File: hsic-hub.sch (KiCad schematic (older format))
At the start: 17 parts

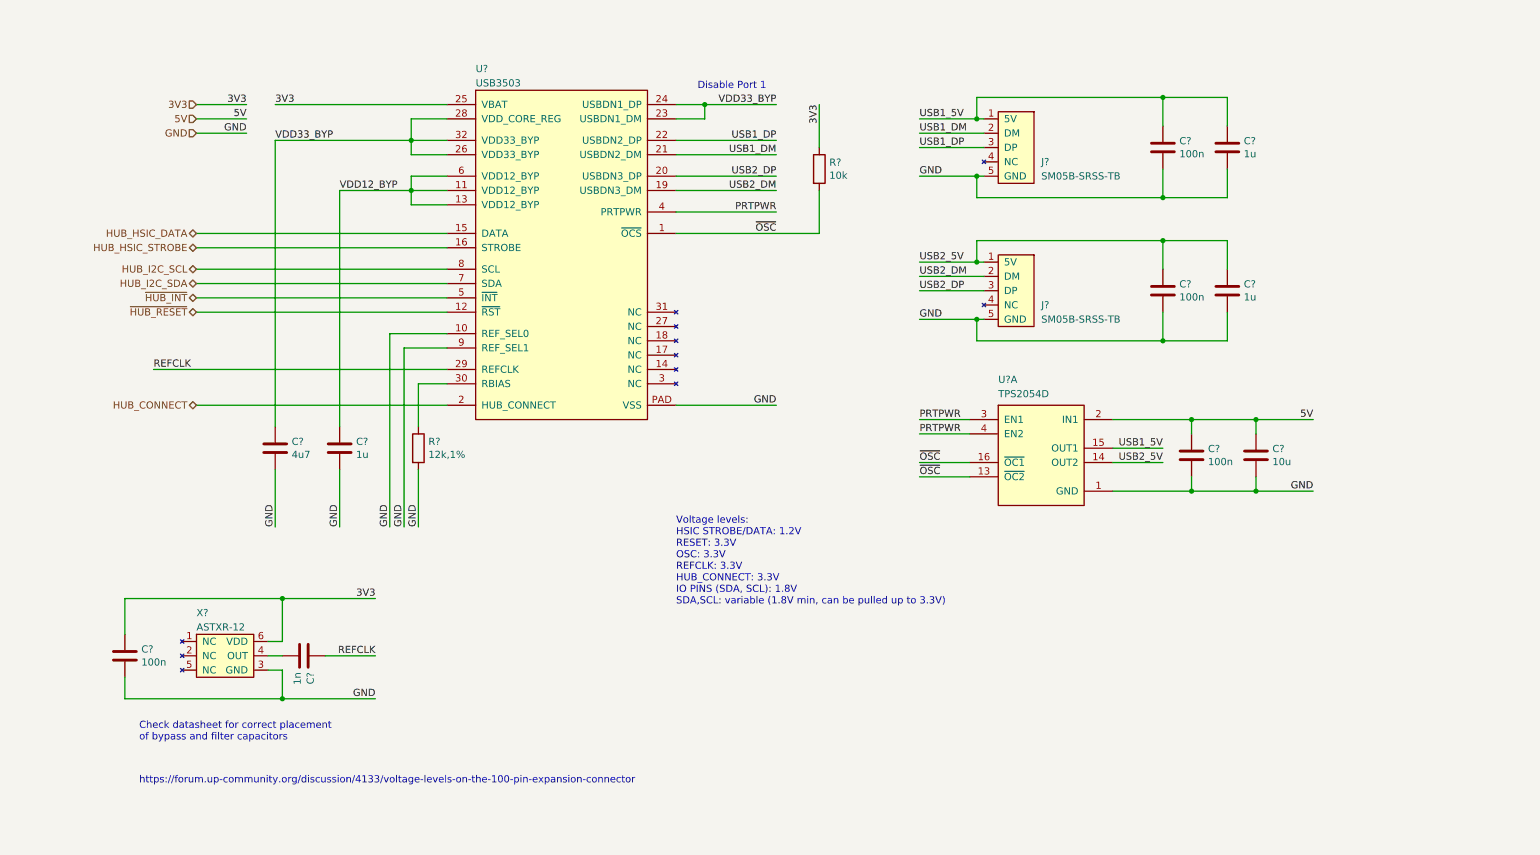
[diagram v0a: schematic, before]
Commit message: Multiple updates. 1. Add MOSFETs to libraries 2. Update HSIC schematic to include level shifting
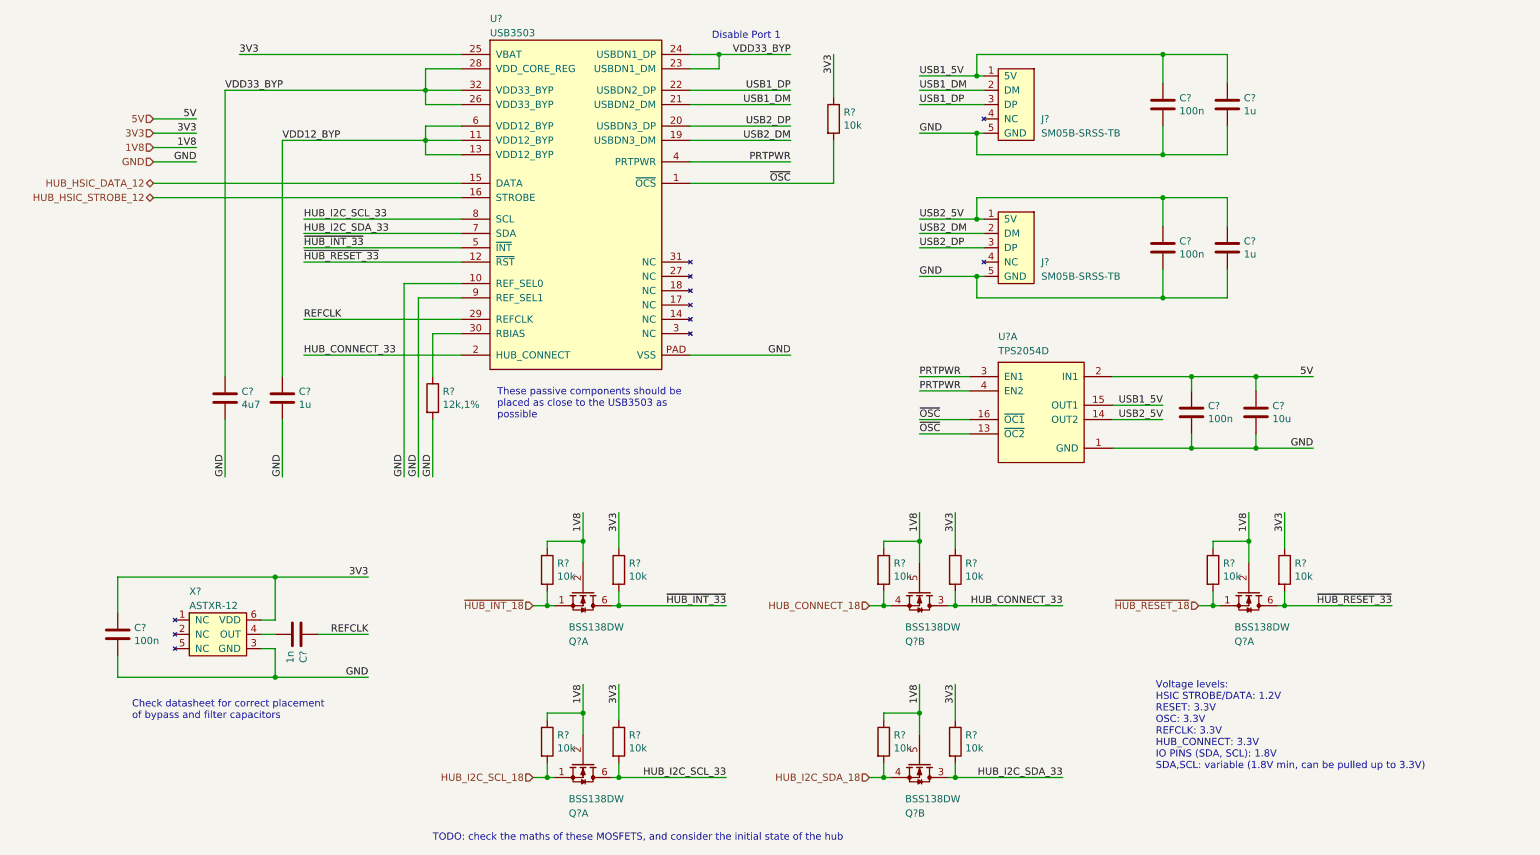
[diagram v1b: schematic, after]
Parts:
- added Q? (x5): BSS138DW, symbol Drone:BSS138DW
- added R? (x10): 10k, symbol Device:R
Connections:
- net 3V3: now also R?.1, R?.1, R?.1, R?.1, R?.1
- net HUB_CONNECT renamed HUB_CONNECT_33
- net HUB_CONNECT_33: now also Q?.3 (D2), R?.2
- net HUB_HSIC_DATA renamed HUB_HSIC_DATA_12
- net HUB_HSIC_STROBE renamed HUB_HSIC_STROBE_12
- net HUB_I2C_SCL renamed HUB_I2C_SCL_33
- net HUB_I2C_SCL_33: now also Q?.6 (D2), R?.2
- net HUB_I2C_SDA renamed HUB_I2C_SDA_33
- net HUB_I2C_SDA_33: now also Q?.3 (D2), R?.2
- net ~HUB_INT renamed ~HUB_INT_33
- net ~HUB_INT_33: now also Q?.6 (D2), R?.2
- net ~HUB_RESET renamed ~HUB_RESET_33
- net ~HUB_RESET_33: now also Q?.6 (D2), R?.2
- new net 1V8: Q?.2 (G2), Q?.2 (G2), Q?.2 (G2), Q?.5 (G2), Q?.5 (G2), R?.1, R?.1, R?.1, R?.1, R?.1
- new net HUB_CONNECT_18: Q?.4 (S2), R?.2
- new net HUB_I2C_SCL_18: Q?.1 (S2), R?.2
- new net HUB_I2C_SDA_18: Q?.4 (S2), R?.2
- new net ~HUB_INT_18: Q?.1 (S2), R?.2
- new net ~HUB_RESET_18: Q?.1 (S2), R?.2
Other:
- note added: "TODO: check the maths of these MOSFETS, and consider the initial state of the hub"
- note added: "These passive components should be\nplaced as close to the USB3503 as\npossible\n"
- note removed: "https://forum.up-community.org/discussion/4133/voltage-levels-on-the-100-pin-expansion-connector"
- moved on the sheet: C?, J?, R?, U?, U?A, X?
